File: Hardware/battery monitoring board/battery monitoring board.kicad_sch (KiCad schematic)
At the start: 3 parts, among them J1 Conn_01x02, J2 Conn_01x02

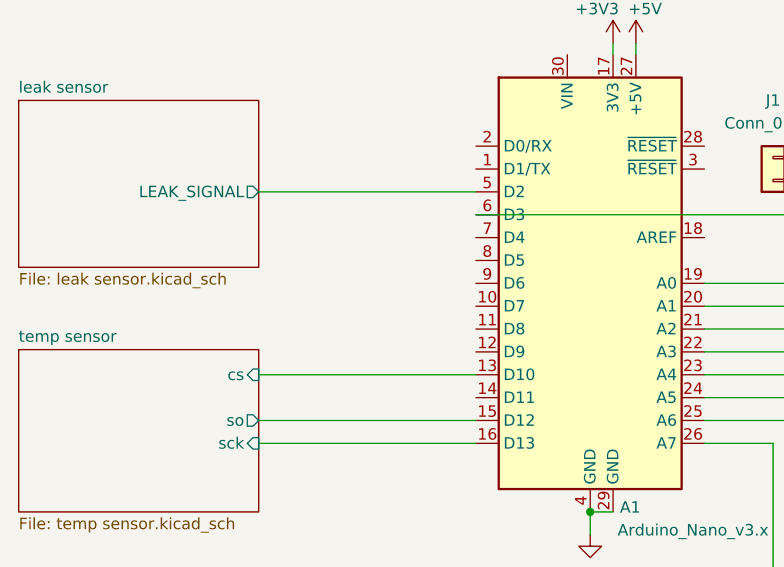
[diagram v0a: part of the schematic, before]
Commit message: added programmable LED and reference updates
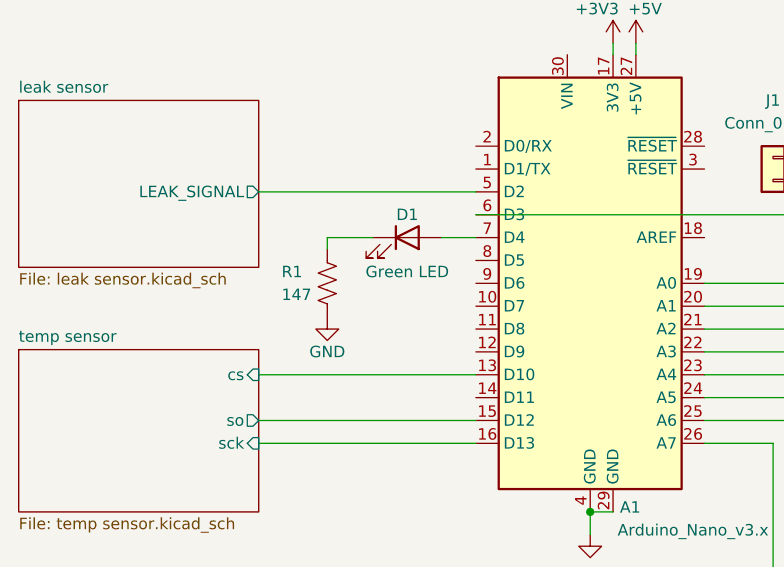
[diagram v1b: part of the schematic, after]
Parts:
- added D1: Green LED, symbol Device:LED
- added R1: 147, symbol Device:R_US
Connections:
- net GND: now also R1.1
- net at A1.7 (D4): now also D1.2 (A)
- new net: D1.1 (K), R1.2
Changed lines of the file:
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@@
+    (stroke (width 0) (type default))
+  )
+  (wire (pts (xy 97.79 80.01) (xy 92.71 80.01))
     (stroke (width 0) (type default))
   )
@@
     (stroke (width 0) (type default))
   )
+  (wire (pts (xy 92.71 80.01) (xy 92.71 81.28))
+    (stroke (width 0) (type default))
+  )
   (wire (pts (xy 144.78 97.79) (xy 144.78 127))
     (stroke (width 0) (type default))
@@
     (stroke (width 0) (type default))
   )
+  (wire (pts (xy 105.41 80.01) (xy 109.22 80.01))
+    (stroke (width 0) (type default))
+  )
   (wire (pts (xy 127 58.42) (xy 127 59.69))
     (stroke (width 0) (type default))
+  )
+  (symbol (lib_id "Device:R_US") (at 92.71 85.09 180) (unit 1)
+    (in_bom yes) (on_board yes) (dnp no)
+    (property "Reference" "R1" (at 87.63 83.82 0)
+      (effects (font (size 1.27 1.27)) (justify right))
+    )
+    (property "Value" "147" (at 87.63 86.36 0)
+      (effects (font (size 1.27 1.27)) (justify right))
+    )
+    (property "Footprint" "" (at 91.694 84.836 90)
+      (effects (font (size 1.27 1.27)) hide)
+    )
+    (property "Datasheet" "~" (at 92.71 85.09 0)
+      (effects (font (size 1.27 1.27)) hide)
+    )
+    (pin "1")
+    (pin "2")
+    (instances
+      (project "battery monitoring board"
+        (path "/bf623d80-ca5a-491f-9daa-4dffbeba5279"
+          (reference "R1") (unit 1)
+        )
+      )
+    )
   )
   (symbol (lib_id "MCU_Module:Arduino_Nano_v3.x") (at 121.92 85.09 0) (unit 1)
@@
   (symbol (lib_id "power:+3V3") (at 124.46 58.42 0) (unit 1)
     (in_bom yes) (on_board yes) (dnp no)
-    (property "Reference" "#PWR02" (at 124.46 62.23 0)
+    (property "Reference" "#PWR03" (at 124.46 62.23 0)
       (effects (font (size 1.27 1.27)) hide)
     )
@@
       (project "battery monitoring board"
         (path "/bf623d80-ca5a-491f-9daa-4dffbeba5279"
-          (reference "#PWR02") (unit 1)
+          (reference "#PWR03") (unit 1)
+        )
+      )
+    )
+  )
+  (symbol (lib_id "Device:LED") (at 101.6 80.01 0) (unit 1)
+    (in_bom yes) (on_board yes) (dnp no)
+    (property "Reference" "D1" (at 101.6 77.47 0)
+      (effects (font (size 1.27 1.27)))
+    )
+    (property "Value" "Green LED" (at 101.6 83.82 0)
+      (effects (font (size 1.27 1.27)))
+    )
+    (property "Footprint" "" (at 101.6 80.01 0)
+      (effects (font (size 1.27 1.27)) hide)
+    )
+    (property "Datasheet" "~" (at 101.6 80.01 0)
+      (effects (font (size 1.27 1.27)) hide)
+    )
+    (pin "1")
+    (pin "2")
+    (instances
+      (project "battery monitoring board"
+        (path "/bf623d80-ca5a-491f-9daa-4dffbeba5279"
+          (reference "D1") (unit 1)
         )
       )
@@
   (symbol (lib_id "PCM_4ms_Power-symbol:GND") (at 191.77 73.66 0) (unit 1)
     (in_bom yes) (on_board yes) (dnp no)
-    (property "Reference" "#PWR05" (at 191.77 80.01 0)
+    (property "Reference" "#PWR06" (at 191.77 80.01 0)
       (effects (font (size 1.27 1.27)) hide)
     )
@@
       (project "battery monitoring board"
         (path "/bf623d80-ca5a-491f-9daa-4dffbeba5279"
-          (reference "#PWR05") (unit 1)
+          (reference "#PWR06") (unit 1)
         )
       )
@@
   (symbol (lib_id "PCM_4ms_Power-symbol:GND") (at 121.92 113.03 0) (unit 1)
     (in_bom yes) (on_board yes) (dnp no) (fields_autoplaced)
-    (property "Reference" "#PWR01" (at 121.92 119.38 0)
+    (property "Reference" "#PWR02" (at 121.92 119.38 0)
       (effects (font (size 1.27 1.27)) hide)
     )
@@
       (project "battery monitoring board"
         (path "/bf623d80-ca5a-491f-9daa-4dffbeba5279"
-          (reference "#PWR01") (unit 1)
+          (reference "#PWR02") (unit 1)
         )
       )
@@
     )
   )
+  (symbol (lib_id "PCM_4ms_Power-symbol:GND") (at 92.71 88.9 0) (unit 1)
+    (in_bom yes) (on_board yes) (dnp no)
+    (property "Reference" "#PWR01" (at 92.71 95.25 0)
+      (effects (font (size 1.27 1.27)) hide)
+    )
+    (property "Value" "GND" (at 92.71 92.71 0)
+      (effects (font (size 1.27 1.27)))
+    )
+    (property "Footprint" "" (at 92.71 88.9 0)
+      (effects (font (size 1.27 1.27)) hide)
+    )
+    (property "Datasheet" "" (at 92.71 88.9 0)
+      (effects (font (size 1.27 1.27)) hide)
+    )
+    (pin "1")
+    (instances
+      (project "battery monitoring board"
+        (path "/bf623d80-ca5a-491f-9daa-4dffbeba5279"
+          (reference "#PWR01") (unit 1)
+        )
+      )
+    )
+  )
   (symbol (lib_id "PCM_4ms_Power-symbol:+5V") (at 127 58.42 0) (unit 1)
     (in_bom yes) (on_board yes) (dnp no)
-    (property "Reference" "#PWR03" (at 127 62.23 0)
+    (property "Reference" "#PWR04" (at 127 62.23 0)
       (effects (font (size 1.27 1.27)) hide)
     )
@@
       (project "battery monitoring board"
         (path "/bf623d80-ca5a-491f-9daa-4dffbeba5279"
-          (reference "#PWR03") (unit 1)
+          (reference "#PWR04") (unit 1)
         )
       )
@@
   (symbol (lib_id "PCM_4ms_Power-symbol:GND") (at 147.32 73.66 0) (unit 1)
     (in_bom yes) (on_board yes) (dnp no)
-    (property "Reference" "#PWR04" (at 147.32 80.01 0)
+    (property "Reference" "#PWR05" (at 147.32 80.01 0)
       (effects (font (size 1.27 1.27)) hide)
     )
@@
       (project "battery monitoring board"
         (path "/bf623d80-ca5a-491f-9daa-4dffbeba5279"
-          (reference "#PWR04") (unit 1)
-        )
-      )
+          (reference "#PWR05") (unit 1)
+        )
+      )

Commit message: Added footprints to battery monitoring
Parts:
- D1: footprint (none) -> Diode_SMD:D_0805_2012Metric_Pad1.15x1.40mm_HandSolder
- J1, J2: footprint (none) -> Library:Power Supply Pads
- R1: footprint (none) -> Resistor_SMD:R_0805_2012Metric_Pad1.20x1.40mm_HandSolder
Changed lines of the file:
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@@
       (effects (font (size 1.27 1.27)) (justify right))
     )
-    (property "Footprint" "" (at 91.694 84.836 90)
+    (property "Footprint" "Resistor_SMD:R_0805_2012Metric_Pad1.20x1.40mm_HandSolder" (at 91.694 84.836 90)
       (effects (font (size 1.27 1.27)) hide)
     )
@@
       (effects (font (size 1.27 1.27)) (justify left))
     )
-    (property "Footprint" "" (at 196.85 71.12 0)
+    (property "Footprint" "Library:Power Supply Pads" (at 196.85 71.12 0)
       (effects (font (size 1.27 1.27)) hide)
     )
@@
       (effects (font (size 1.27 1.27)))
     )
-    (property "Footprint" "" (at 101.6 80.01 0)
+    (property "Footprint" "Diode_SMD:D_0805_2012Metric_Pad1.15x1.40mm_HandSolder" (at 101.6 80.01 0)
       (effects (font (size 1.27 1.27)) hide)
     )
@@
       (effects (font (size 1.27 1.27)))
     )
-    (property "Footprint" "" (at 142.24 73.66 0)
+    (property "Footprint" "Library:Power Supply Pads" (at 142.24 73.66 0)
       (effects (font (size 1.27 1.27)) hide)
     )

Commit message: silkscreen
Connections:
- net +9V: now reaches A1.30 (VIN)
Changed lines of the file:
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@@
+    (stroke (width 0) (type default))
+  )
+  (wire (pts (xy 119.38 58.42) (xy 119.38 59.69))
     (stroke (width 0) (type default))
   )
@@
         )
       )
+    )
+  )
+  (symbol (lib_id "PCM_4ms_Power-symbol:+9V") (at 119.38 58.42 0) (unit 1)
+    (in_bom yes) (on_board yes) (dnp no)
+    (property "Reference" "#PWR030" (at 119.38 62.23 0)
+      (effects (font (size 1.27 1.27)) hide)
+    )
+    (property "Value" "+9V" (at 119.38 54.61 0)
+      (effects (font (size 1.27 1.27)))
+    )
+    (property "Footprint" "" (at 119.38 58.42 0)
+      (effects (font (size 1.27 1.27)) hide)
+    )
+    (property "Datasheet" "" (at 119.38 58.42 0)
+      (effects (font (size 1.27 1.27)) hide)
+    )
+    (pin "1")
+    (instances
+      (project "battery monitoring board"
+        (path "/bf623d80-ca5a-491f-9daa-4dffbeba5279/d1e89632-1041-42ed-815d-03472eda859a"
+          (reference "#PWR030") (unit 1)
+        )
+        (path "/bf623d80-ca5a-491f-9daa-4dffbeba5279"
+          (reference "#PWR031") (unit 1)
+        )
+      )

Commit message: Added adc to schematic
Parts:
- added D6, D7: Green LED, Diode_SMD:D_0805_2012Metric_Pad1.15x1.40mm_HandSolder, symbol Device:LED
- added R24, R25: 147, Resistor_SMD:R_0805_2012Metric_Pad1.20x1.40mm_HandSolder, symbol Device:R_US
- added U2: MCP3008, symbol Analog_ADC:MCP3008
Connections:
- net +5V: now also U2.15 (Vref), U2.16 (Vdd)
- net GND: now also R24.1, R25.1, U2.14 (AGND), U2.9 (DGND)
- net temp sensor/sck: now also U2.13 (CLK)
- net temp sensor/so: now also U2.12 (Dout)
- net voltage monitor/OUT1: now also U2.1 (CH0); no longer A1.19 (A0)
- net voltage monitor/OUT2: now also U2.2 (CH1); no longer A1.20 (A1)
- net voltage monitor/OUT3: now also U2.3 (CH2); no longer A1.21 (A2)
- net voltage monitor/OUT4: now also U2.4 (CH3); no longer A1.22 (A3)
- net voltage monitor2/OUT1: now also U2.5 (CH4); no longer A1.23 (A4)
- net voltage monitor2/OUT2: now also U2.6 (CH5); no longer A1.24 (A5)
- net voltage monitor2/OUT3: now also U2.7 (CH6); no longer A1.25 (A6)
- net voltage monitor2/OUT4: now also U2.8 (CH7); no longer A1.26 (A7)
- net at A1.12 (D9): now also U2.10 (~{CS}/SHDN)
- net at A1.14 (D11): now also U2.11 (Din)
- net at A1.8 (D5): now also D6.2 (A)
- net at A1.9 (D6): now also D7.2 (A)
- new net: D7.1 (K), R25.2
- new net: D6.1 (K), R24.2
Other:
- moved on the sheet: D1, R1

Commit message: updated battery board pt.II
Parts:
- removed D7: Green LED, Diode_SMD:D_0805_2012Metric_Pad1.15x1.40mm_HandSolder, symbol Device:LED
- removed R25: 147, Resistor_SMD:R_0805_2012Metric_Pad1.20x1.40mm_HandSolder, symbol Device:R_US
- R1: value 147 -> 150
- R2: renamed from R24; value 147 -> 150
- U1: renamed from U2; footprint (none) -> PCM_Package_SO_AKL:SOIC-16_3.9x9.9mm_P1.27mm
- renumbered D6 to D2

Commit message: finalized battery board !!
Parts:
- added C3: 100nF, Capacitor_SMD:C_0805_2012Metric_Pad1.18x1.45mm_HandSolder, symbol Device:C
- added R10: 10k, Resistor_SMD:R_0805_2012Metric_Pad1.20x1.40mm_HandSolder, symbol Device:R_US
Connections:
- net +5V: now also C3.1, R10.2
- net GND: now also C3.2
- net at A1.12 (D9), U1.10 (~{CS}/SHDN): now also R10.1
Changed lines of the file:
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@@
 (kicad_sch (version 20230121) (generator eeschema)
   (paper "A4")
+  (junction (at 99.06 139.7) (diameter 0) (color 0 0 0 0)
+  )
   (junction (at 102.87 100.33) (diameter 0) (color 0 0 0 0)
   )
@@
     (stroke (width 0) (type default))
   )
+  (wire (pts (xy 99.06 139.7) (xy 105.41 139.7))
+    (stroke (width 0) (type default))
+  )
   (wire (pts (xy 95.25 134.62) (xy 102.87 134.62))
     (stroke (width 0) (type default))
@@
     (stroke (width 0) (type default))
   )
+  (wire (pts (xy 99.06 149.86) (xy 99.06 147.32))
+    (stroke (width 0) (type default))
+  )
   (wire (pts (xy 88.9 58.42) (xy 87.63 58.42))
     (stroke (width 0) (type default))
@@
     (stroke (width 0) (type default))
   )
-  (wire (pts (xy 95.25 139.7) (xy 105.41 139.7))
+  (wire (pts (xy 95.25 139.7) (xy 99.06 139.7))
     (stroke (width 0) (type default))
   )
@@
     )
   )
+  (symbol (lib_id "Device:R_US") (at 99.06 143.51 0) (unit 1)
+    (in_bom yes) (on_board yes) (dnp no) (fields_autoplaced)
+    (property "Reference" "R10" (at 101.6 142.24 0)
+      (effects (font (size 1.27 1.27)) (justify left))
+    )
+    (property "Value" "10k" (at 101.6 144.78 0)
+      (effects (font (size 1.27 1.27)) (justify left))
+    )
+    (property "Footprint" "Resistor_SMD:R_0805_2012Metric_Pad1.20x1.40mm_HandSolder" (at 100.076 143.764 90)
+      (effects (font (size 1.27 1.27)) hide)
+    )
+    (property "Datasheet" "~" (at 99.06 143.51 0)
+      (effects (font (size 1.27 1.27)) hide)
+    )
+    (pin "1")
+    (pin "2")
+    (instances
+      (project "battery monitoring board"
+        (path "/bf623d80-ca5a-491f-9daa-4dffbeba5279/5ec2dbdf-a276-4d4c-99fc-008475c1e770"
+          (reference "R10") (unit 1)
+        )
+        (path "/bf623d80-ca5a-491f-9daa-4dffbeba5279"
+          (reference "R26") (unit 1)
+        )
+      )
+    )
+  )
   (symbol (lib_id "power:+3V3") (at 124.46 58.42 0) (unit 1)
     (in_bom yes) (on_board yes) (dnp no)
-    (property "Reference" "#PWR09" (at 124.46 62.23 0)
+    (property "Reference" "#PWR010" (at 124.46 62.23 0)
       (effects (font (size 1.27 1.27)) hide)
     )
@@
       (project "battery monitoring board"
         (path "/bf623d80-ca5a-491f-9daa-4dffbeba5279"
-          (reference "#PWR09") (unit 1)
+          (reference "#PWR010") (unit 1)
+        )
+      )
+    )
+  )
+  (symbol (lib_id "PCM_4ms_Power-symbol:+5V") (at 99.06 149.86 180) (unit 1)
+    (in_bom yes) (on_board yes) (dnp no)
+    (property "Reference" "#PWR038" (at 99.06 146.05 0)
+      (effects (font (size 1.27 1.27)) hide)
+    )
+    (property "Value" "+5V" (at 98.044 153.67 0)
+      (effects (font (size 1.27 1.27)))
+    )
+    (property "Footprint" "" (at 99.06 149.86 0)
+      (effects (font (size 1.27 1.27)) hide)
+    )
+    (property "Datasheet" "" (at 99.06 149.86 0)
+      (effects (font (size 1.27 1.27)) hide)
+    )
+    (pin "1")
+    (instances
+      (project "battery monitoring board"
+        (path "/bf623d80-ca5a-491f-9daa-4dffbeba5279"
+          (reference "#PWR038") (unit 1)
         )
       )
@@
         )
         (path "/bf623d80-ca5a-491f-9daa-4dffbeba5279"
-          (reference "#PWR07") (unit 1)
+          (reference "#PWR08") (unit 1)
         )
       )
@@
     )
   )
+  (symbol (lib_id "PCM_4ms_Power-symbol:+5V") (at 109.22 142.24 0) (unit 1)
+    (in_bom yes) (on_board yes) (dnp no)
+    (property "Reference" "#PWR06" (at 109.22 146.05 0)
+      (effects (font (size 1.27 1.27)) hide)
+    )
+    (property "Value" "+5V" (at 110.236 138.43 0)
+      (effects (font (size 1.27 1.27)))
+    )
+    (property "Footprint" "" (at 109.22 142.24 0)
+      (effects (font (size 1.27 1.27)) hide)
+    )
+    (property "Datasheet" "" (at 109.22 142.24 0)
+      (effects (font (size 1.27 1.27)) hide)
+    )
+    (pin "1")
+    (instances
+      (project "battery monitoring board"
+        (path "/bf623d80-ca5a-491f-9daa-4dffbeba5279"
+          (reference "#PWR06") (unit 1)
+        )
+      )
+    )
+  )
   (symbol (lib_id "Device:LED") (at 100.33 49.53 0) (unit 1)
     (in_bom yes) (on_board yes) (dnp no)
@@
     )
   )
+  (symbol (lib_id "Device:C") (at 109.22 146.05 0) (unit 1)
+    (in_bom yes) (on_board yes) (dnp no)
+    (property "Reference" "C3" (at 113.03 144.78 0)
+      (effects (font (size 1.27 1.27)) (justify left))
+    )
+    (property "Value" "100nF" (at 113.03 147.32 0)
+      (effects (font (size 1.27 1.27)) (justify left))
+    )
+    (property "Footprint" "Capacitor_SMD:C_0805_2012Metric_Pad1.18x1.45mm_HandSolder" (at 110.1852 149.86 0)
+      (effects (font (size 1.27 1.27)) hide)
+    )
+    (property "Datasheet" "~" (at 109.22 146.05 0)
+      (effects (font (size 1.27 1.27)) hide)
+    )
+    (pin "1")
+    (pin "2")
+    (instances
+      (project "voltage monitor"
+        (path "/64dd58dd-0f80-4046-8958-33031e8c772b"
+          (reference "C3") (unit 1)
+        )
+      )
+      (project "battery monitoring board"
+        (path "/bf623d80-ca5a-491f-9daa-4dffbeba5279/986cc9e1-c37e-4aa2-b3b5-8e2dcbe750c5"
+          (reference "C1") (unit 1)
+        )
+        (path "/bf623d80-ca5a-491f-9daa-4dffbeba5279/26c6129c-8fb5-4658-8c7a-1dc4298981ba"
+          (reference "C8") (unit 1)
+        )
+        (path "/bf623d80-ca5a-491f-9daa-4dffbeba5279"
+          (reference "C1") (unit 1)
+        )
+      )
+    )
+  )
   (symbol (lib_id "PCM_4ms_Power-symbol:GND") (at 191.77 73.66 0) (unit 1)
     (in_bom yes) (on_board yes) (dnp no)
-    (property "Reference" "#PWR012" (at 191.77 80.01 0)
+    (property "Reference" "#PWR013" (at 191.77 80.01 0)
       (effects (font (size 1.27 1.27)) hide)
     )
@@
       (project "battery monitoring board"
         (path "/bf623d80-ca5a-491f-9daa-4dffbeba5279"
-          (reference "#PWR012") (unit 1)
+          (reference "#PWR013") (unit 1)
         )
       )
@@
   (symbol (lib_id "PCM_4ms_Power-symbol:GND") (at 121.92 113.03 0) (unit 1)
     (in_bom yes) (on_board yes) (dnp no) (fields_autoplaced)
-    (property "Reference" "#PWR08" (at 121.92 119.38 0)
+    (property "Reference" "#PWR09" (at 121.92 119.38 0)
       (effects (font (size 1.27 1.27)) hide)
     )
@@
       (project "battery monitoring board"
         (path "/bf623d80-ca5a-491f-9daa-4dffbeba5279"
-          (reference "#PWR08") (unit 1)
+          (reference "#PWR09") (unit 1)
         )
       )
@@
   (symbol (lib_id "PCM_4ms_Power-symbol:+5V") (at 127 58.42 0) (unit 1)
     (in_bom yes) (on_board yes) (dnp no)
-    (property "Reference" "#PWR010" (at 127 62.23 0)
+    (property "Reference" "#PWR011" (at 127 62.23 0)
       (effects (font (size 1.27 1.27)) hide)
     )
@@
       (project "battery monitoring board"
         (path "/bf623d80-ca5a-491f-9daa-4dffbeba5279"
-          (reference "#PWR010") (unit 1)
+          (reference "#PWR011") (unit 1)
         )
       )
@@
   (symbol (lib_id "PCM_4ms_Power-symbol:GND") (at 147.32 73.66 0) (unit 1)
     (in_bom yes) (on_board yes) (dnp no)
-    (property "Reference" "#PWR011" (at 147.32 80.01 0)
+    (property "Reference" "#PWR012" (at 147.32 80.01 0)
       (effects (font (size 1.27 1.27)) hide)
     )
@@
       (project "battery monitoring board"
         (path "/bf623d80-ca5a-491f-9daa-4dffbeba5279"
-          (reference "#PWR011") (unit 1)
-        )
-      )
+          (reference "#PWR012") (unit 1)
+        )
+      )
+    )
+  )
+  (symbol (lib_id "PCM_4ms_Power-symbol:GND") (at 109.22 149.86 0) (unit 1)
+    (in_bom yes) (on_board yes) (dnp no) (fields_autoplaced)
+    (property "Reference" "#PWR07" (at 109.22 156.21 0)
+      (effects (font (size 1.27 1.27)) hide)
+    )
+    (property "Value" "GND" (at 109.22 154.432 0)
+      (effects (font (size 1.27 1.27)))
+    )
+    (property "Footprint" "" (at 109.22 149.86 0)
+      (effects (font (size 1.27 1.27)) hide)
+    )
+    (property "Datasheet" "" (at 109.22 149.86 0)
+      (effects (font (size 1.27 1.27)) hide)
+    )
+    (pin "1")
+    (instances
+      (project "battery monitoring board"
+        (path "/bf623d80-ca5a-491f-9daa-4dffbeba5279"
+          (reference "#PWR07") (unit 1)
+        )
+      )
